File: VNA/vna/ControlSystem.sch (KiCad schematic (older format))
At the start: 29 parts, among them J5 ICSP 1,3,5, J6 ICSP 2,4,6, J7 Bluetooth Module Socket, J8 tx_d12, J9 vin_d13, SW1 Reset, U7 FT232RL, U8 ATmega328PB-AU, Y1 16MHz

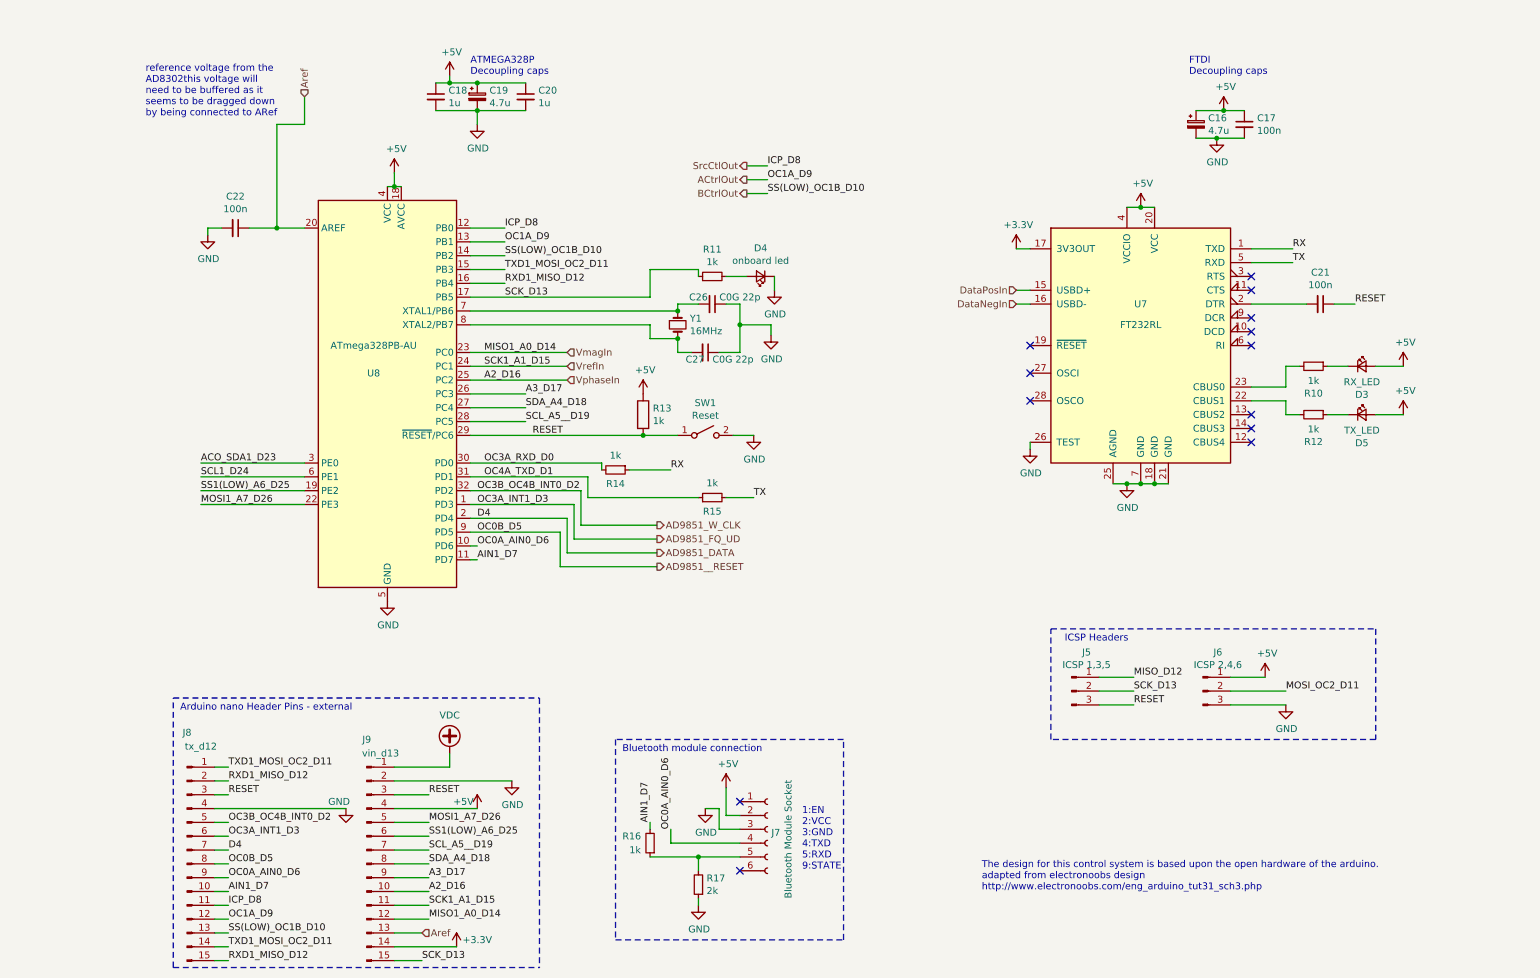
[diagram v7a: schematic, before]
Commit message: initial pcb design
initial layout and grouping of components complete
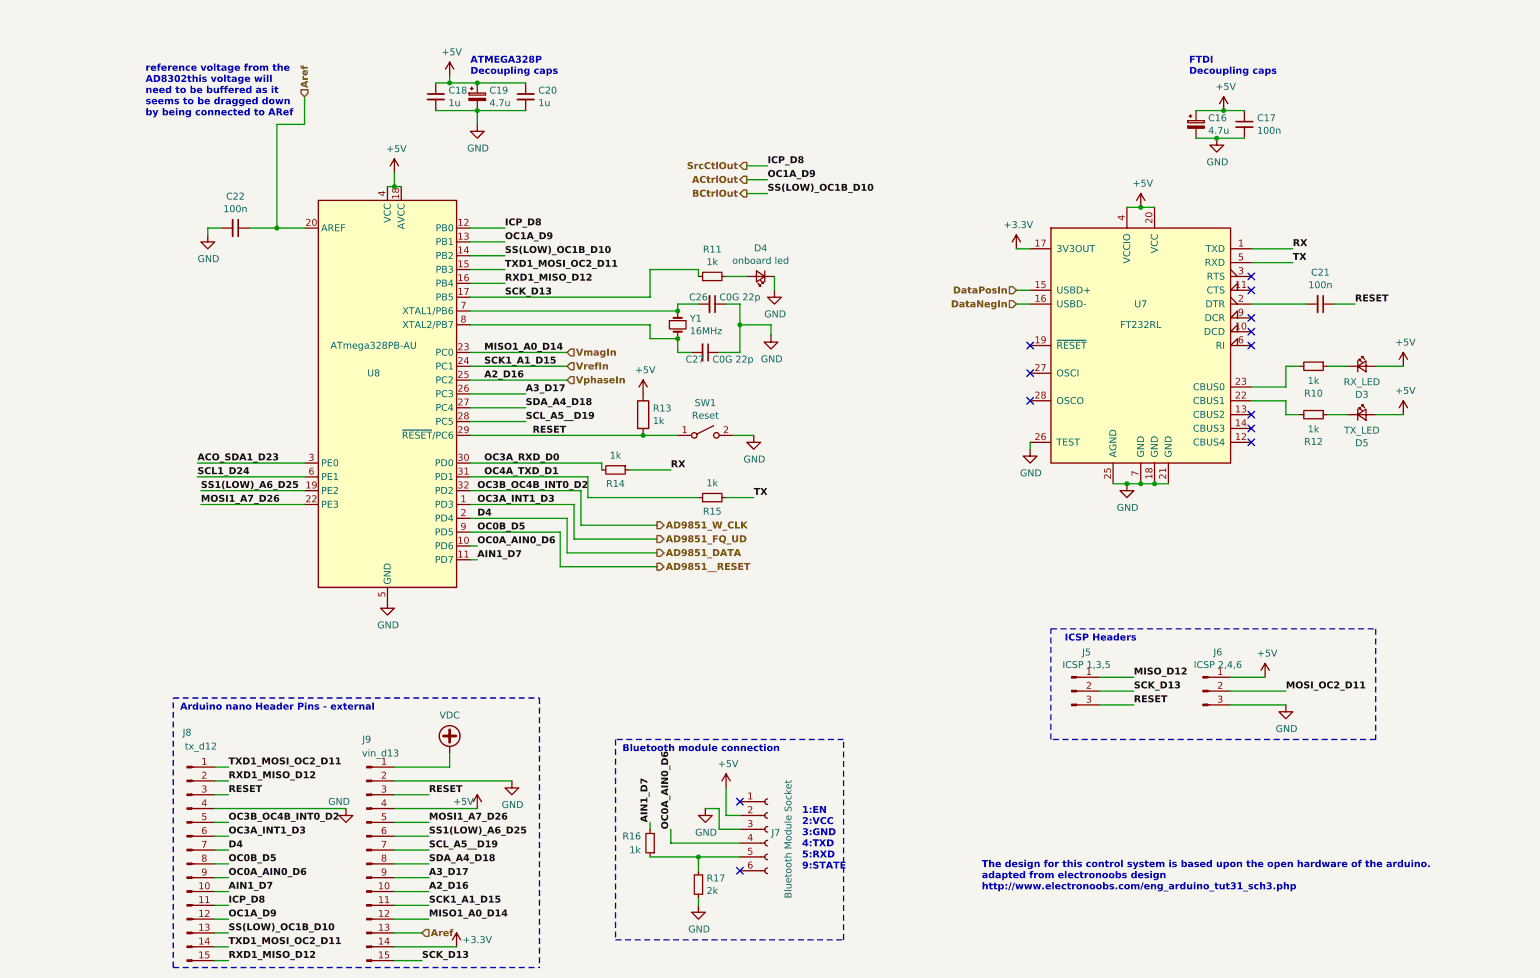
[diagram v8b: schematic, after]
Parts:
- C17, C18, C20, C21, C22, C26, C27: footprint Capacitor_SMD:C_1206_3216Metric_Pad1.42x1.75mm_HandSolder -> Capacitor_SMD:C_0805_2012Metric_Pad1.15x1.40mm_HandSolder
- R10, R11, R12, R13, R14, R15, R16, R17: footprint Resistor_SMD:R_1206_3216Metric_Pad1.42x1.75mm_HandSolder -> Resistor_SMD:R_0805_2012Metric_Pad1.15x1.40mm_HandSolder
